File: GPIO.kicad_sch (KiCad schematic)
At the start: 18 parts, among them U1 74LS245

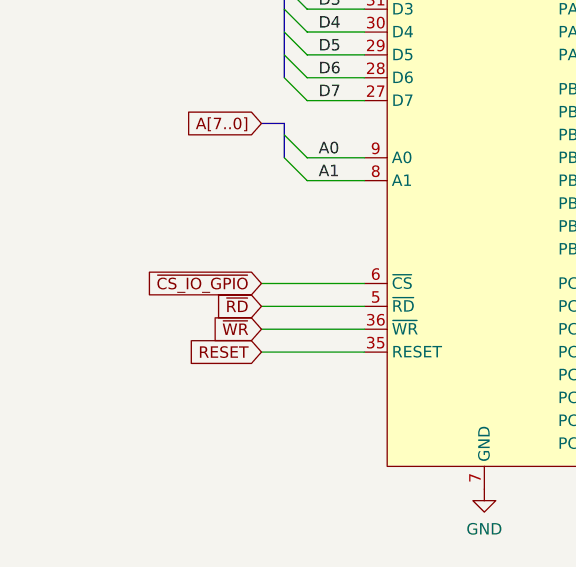
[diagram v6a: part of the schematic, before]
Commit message: IO space: wire renaming
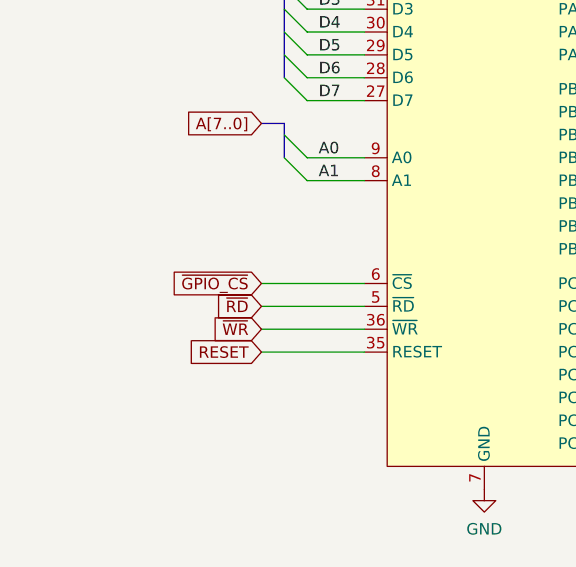
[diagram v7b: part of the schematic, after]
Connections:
- net ~{CS_IO_GPIO} renamed ~{GPIO_CS}
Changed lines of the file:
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@@
+    )
+  )
+  (global_label "~{GPIO_CS}" (shape input) (at 34.29 73.66 180) (fields_autoplaced)
+    (effects (font (size 1.27 1.27)) (justify right))
+    (property "Intersheetrefs" "${INTERSHEET_REFS}" (at 23.3824 73.66 0)
+      (effects (font (size 1.27 1.27)) (justify right) hide)
     )
   )
@@
       (effects (font (size 1.27 1.27)) (justify right) hide)
     )
-  )
-  (global_label "~{CS_IO_GPIO}" (shape input) (at 34.29 73.66 180) (fields_autoplaced)
-    (effects (font (size 1.27 1.27)) (justify right))
-    (property "Intersheetrefs" "${INTERSHEET_REFS}" (at 20.4795 73.66 0)
-      (effects (font (size 1.27 1.27)) (justify right) hide)
-    )

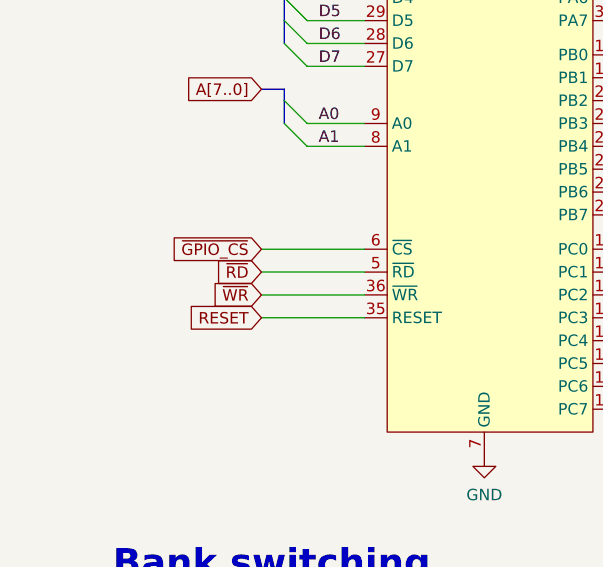
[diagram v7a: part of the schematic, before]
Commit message: Typo fixes
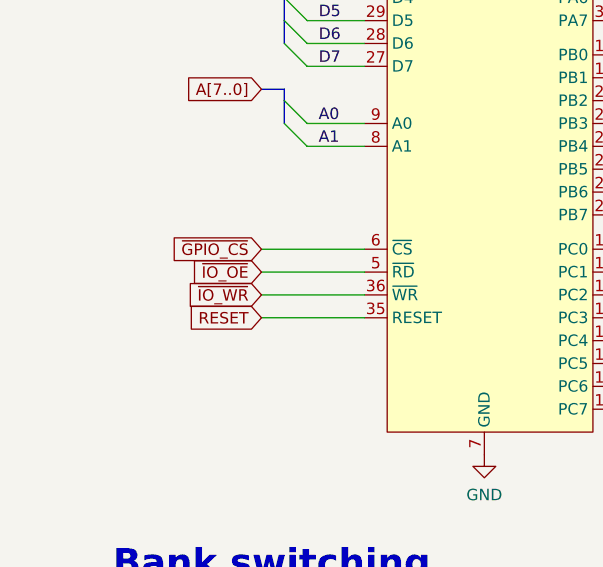
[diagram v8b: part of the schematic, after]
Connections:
- net ~{RD} renamed ~{IO_OE}
- net ~{WR} renamed ~{IO_WR}
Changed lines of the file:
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@@
     )
   )
-  (global_label "~{RD}" (shape input) (at 34.29 76.2 180) (fields_autoplaced)
+  (global_label "~{IO_OE}" (shape input) (at 34.29 76.2 180) (fields_autoplaced)
     (effects (font (size 1.27 1.27)) (justify right))
-    (property "Intersheetrefs" "${INTERSHEET_REFS}" (at 28.7648 76.2 0)
+    (property "Intersheetrefs" "${INTERSHEET_REFS}" (at 25.9224 76.2 0)
       (effects (font (size 1.27 1.27)) (justify right) hide)
     )
   )
-  (global_label "~{WR}" (shape input) (at 34.29 78.74 180) (fields_autoplaced)
+  (global_label "~{IO_WR}" (shape input) (at 34.29 78.74 180) (fields_autoplaced)
     (effects (font (size 1.27 1.27)) (justify right))
-    (property "Intersheetrefs" "${INTERSHEET_REFS}" (at 28.5834 78.74 0)
+    (property "Intersheetrefs" "${INTERSHEET_REFS}" (at 25.6805 78.74 0)
       (effects (font (size 1.27 1.27)) (justify right) hide)
     )
